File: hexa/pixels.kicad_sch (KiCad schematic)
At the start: 171 parts

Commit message: make the lipo_parallel pcb taller to fit everything better; lipo_parallel layout concept for battery terminals on the same side - change pin-matchups to work with that better; make motionhexa larger (more pixels) to accomodate that and bc more pixels = better; insert some capacitors with layout script
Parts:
- removed D76, D77, D78, D79: SK9822-EC20, motionhexa:LED-SK9822-EC20, symbol motionhexa:LED-SK9822-EC20
- added C10, C11, C12, C3, C4, C5, C6, C7, C8, C9: 1u, Capacitor_SMD:C_0402_1005Metric, symbol Device:C_Small
- added D166, D167, D168, D169, D170, D171, D172, D173, D174, D175, D176, D177, D178, D179, D180, D181, D182, D183, D184, D185, D186, D187, D188, D189, D190, D191, D192, D193, D194, D195, D196, D197, D198, D199, D200, D201, D202, D203, D204, D205, D206, D207, D208, D209, D210, D211, D212, D213, D214, D215, D216, D217, D218, D219, D220, D221, D222, D223, D224, D225, D226, D227, D228, D229, D230, D231, D232, D233, D234, D235, D236, D237, D238, D239, D240, D241, D242, D243, D244, D245, D246, D247, D248, D249, D250, D251, D252, D253, D254, D255, D256, D257, D258, D259, D260, D261, D262, D263, D264, D265, D266, D267, D268, D269, D270, D271: SK9822-EC20, motionhexa:LED-SK9822-EC20, symbol motionhexa:LED-SK9822-EC20
- C20, C21: value 10u -> 1u
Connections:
- net +5V: now also C10.1, C11.1, C12.1, C3.1, C4.1, C5.1, C6.1, C7.1, C8.1, C9.1, D166.5 (VDD), D167.5 (VDD), D168.5 (VDD), D169.5 (VDD), D170.5 (VDD), D171.5 (VDD), D172.5 (VDD), D173.5 (VDD), D174.5 (VDD), D175.5 (VDD), D176.5 (VDD), D177.5 (VDD), D178.5 (VDD), D179.5 (VDD), D180.5 (VDD), D181.5 (VDD), D182.5 (VDD), D183.5 (VDD), D184.5 (VDD), D185.5 (VDD), D186.5 (VDD), D187.5 (VDD), D188.5 (VDD), D189.5 (VDD), D190.5 (VDD), D191.5 (VDD), D192.5 (VDD), D193.5 (VDD), D194.5 (VDD), D195.5 (VDD)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
- net GND: now also C10.2, C11.2, C12.2, C3.2, C4.2, C5.2, C6.2, C7.2, C8.2, C9.2, D166.2 (GND), D167.2 (GND), D168.2 (GND), D169.2 (GND), D170.2 (GND), D171.2 (GND), D172.2 (GND), D173.2 (GND), D174.2 (GND), D175.2 (GND), D176.2 (GND), D177.2 (GND), D178.2 (GND), D179.2 (GND), D180.2 (GND), D181.2 (GND), D182.2 (GND), D183.2 (GND), D184.2 (GND), D185.2 (GND), D186.2 (GND), D187.2 (GND), D188.2 (GND), D189.2 (GND), D190.2 (GND), D191.2 (GND), D192.2 (GND), D193.2 (GND), D194.2 (GND), D195.2 (GND)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
- net at D75.1 (SDO): now also D166.3 (SDI)
- net at D75.6 (CKO): now also D166.4 (CKI)
- new net: D250.1 (SDO), D251.3 (SDI)
- new net: D249.1 (SDO), D250.3 (SDI)
- new net: D249.6 (CKO), D250.4 (CKI)
- new net: D250.6 (CKO), D251.4 (CKI)
- new net: D176.1 (SDO), D177.3 (SDI)
- new net: D175.1 (SDO), D176.3 (SDI)
- new net: D175.6 (CKO), D176.4 (CKI)
- new net: D176.6 (CKO), D177.4 (CKI)
- new net: D168.1 (SDO), D169.3 (SDI)
- new net: D167.1 (SDO), D168.3 (SDI)
- new net: D167.6 (CKO), D168.4 (CKI)
- new net: D168.6 (CKO), D169.4 (CKI)
- new net: D195.1 (SDO), D196.3 (SDI)
- new net: D194.1 (SDO), D195.3 (SDI)
- new net: D194.6 (CKO), D195.4 (CKI)
- new net: D195.6 (CKO), D196.4 (CKI)
- new net: D191.1 (SDO), D192.3 (SDI)
- new net: D190.1 (SDO), D191.3 (SDI)
- new net: D190.6 (CKO), D191.4 (CKI)
- new net: D191.6 (CKO), D192.4 (CKI)
- new net: D229.1 (SDO), D230.3 (SDI)
- new net: D228.1 (SDO), D229.3 (SDI)
- new net: D228.6 (CKO), D229.4 (CKI)
- new net: D229.6 (CKO), D230.4 (CKI)
- new net: D204.1 (SDO), D205.3 (SDI)
- new net: D203.1 (SDO), D204.3 (SDI)
- new net: D203.6 (CKO), D204.4 (CKI)
- new net: D204.6 (CKO), D205.4 (CKI)
- new net: D237.1 (SDO), D238.3 (SDI)
- new net: D236.1 (SDO), D237.3 (SDI)
- new net: D236.6 (CKO), D237.4 (CKI)
- new net: D237.6 (CKO), D238.4 (CKI)
- new net: D182.1 (SDO), D183.3 (SDI)
- new net: D181.1 (SDO), D182.3 (SDI)
- new net: D181.6 (CKO), D182.4 (CKI)
- new net: D182.6 (CKO), D183.4 (CKI)
- new net: D262.1 (SDO), D263.3 (SDI)
- new net: D261.1 (SDO), D262.3 (SDI)
- new net: D261.6 (CKO), D262.4 (CKI)
- new net: D262.6 (CKO), D263.4 (CKI)
- new net: D227.1 (SDO), D228.3 (SDI)
- new net: D227.6 (CKO), D228.4 (CKI)
- new net: D189.1 (SDO), D190.3 (SDI)
- new net: D189.6 (CKO), D190.4 (CKI)
- new net: D251.1 (SDO), D252.3 (SDI)
- new net: D251.6 (CKO), D252.4 (CKI)
- new net: D208.1 (SDO), D209.3 (SDI)
- new net: D207.1 (SDO), D208.3 (SDI)
- new net: D207.6 (CKO), D208.4 (CKI)
- new net: D208.6 (CKO), D209.4 (CKI)
- new net: D263.1 (SDO), D264.3 (SDI)
- new net: D263.6 (CKO), D264.4 (CKI)
- new net: D180.1 (SDO), D181.3 (SDI)
- new net: D179.1 (SDO), D180.3 (SDI)
- new net: D179.6 (CKO), D180.4 (CKI)
- new net: D180.6 (CKO), D181.4 (CKI)
- new net: D174.1 (SDO), D175.3 (SDI)
- new net: D173.1 (SDO), D174.3 (SDI)
- new net: D173.6 (CKO), D174.4 (CKI)
- new net: D174.6 (CKO), D175.4 (CKI)
- new net: D226.1 (SDO), D227.3 (SDI)
- new net: D225.1 (SDO), D226.3 (SDI)
- new net: D225.6 (CKO), D226.4 (CKI)
- new net: D226.6 (CKO), D227.4 (CKI)
- new net: D212.1 (SDO), D213.3 (SDI)
- new net: D211.1 (SDO), D212.3 (SDI)
- new net: D211.6 (CKO), D212.4 (CKI)
- new net: D212.6 (CKO), D213.4 (CKI)
- new net: D252.1 (SDO), D253.3 (SDI)
- new net: D252.6 (CKO), D253.4 (CKI)
- new net: D184.1 (SDO), D185.3 (SDI)
- new net: D183.1 (SDO), D184.3 (SDI)
- new net: D183.6 (CKO), D184.4 (CKI)
- new net: D184.6 (CKO), D185.4 (CKI)
- new net: D206.1 (SDO), D207.3 (SDI)
- new net: D206.6 (CKO), D207.4 (CKI)
- new net: D177.1 (SDO), D178.3 (SDI)
- new net: D177.6 (CKO), D178.4 (CKI)
- new net: D199.1 (SDO), D200.3 (SDI)
- new net: D198.1 (SDO), D199.3 (SDI)
- new net: D198.6 (CKO), D199.4 (CKI)
- new net: D199.6 (CKO), D200.4 (CKI)
- new net: D178.1 (SDO), D179.3 (SDI)
- new net: D178.6 (CKO), D179.4 (CKI)
- new net: D270.1 (SDO), D271.3 (SDI)
- new net: D269.1 (SDO), D270.3 (SDI)
- new net: D269.6 (CKO), D270.4 (CKI)
- new net: D270.6 (CKO), D271.4 (CKI)
- new net: D217.1 (SDO), D218.3 (SDI)
- new net: D216.1 (SDO), D217.3 (SDI)
- new net: D216.6 (CKO), D217.4 (CKI)
- new net: D217.6 (CKO), D218.4 (CKI)
- new net: D210.1 (SDO), D211.3 (SDI)
- new net: D210.6 (CKO), D211.4 (CKI)
- new net: D224.1 (SDO), D225.3 (SDI)
- new net: D224.6 (CKO), D225.4 (CKI)
- new net: D240.1 (SDO), D241.3 (SDI)
- new net: D239.1 (SDO), D240.3 (SDI)
- new net: D239.6 (CKO), D240.4 (CKI)
- new net: D240.6 (CKO), D241.4 (CKI)
- new net: D197.1 (SDO), D198.3 (SDI)
- new net: D197.6 (CKO), D198.4 (CKI)
- new net: D253.1 (SDO), D254.3 (SDI)
- new net: D253.6 (CKO), D254.4 (CKI)
- new net: D213.1 (SDO), D214.3 (SDI)
- new net: D213.6 (CKO), D214.4 (CKI)
- new net: D266.1 (SDO), D267.3 (SDI)
- new net: D265.1 (SDO), D266.3 (SDI)
- new net: D265.6 (CKO), D266.4 (CKI)
- new net: D266.6 (CKO), D267.4 (CKI)
- new net: D268.1 (SDO), D269.3 (SDI)
- new net: D268.6 (CKO), D269.4 (CKI)
- new net: D231.1 (SDO), D232.3 (SDI)
- new net: D230.1 (SDO), D231.3 (SDI)
- new net: D230.6 (CKO), D231.4 (CKI)
- new net: D231.6 (CKO), D232.4 (CKI)
- new net: D166.1 (SDO), D167.3 (SDI)
- new net: D166.6 (CKO), D167.4 (CKI)
- new net: D259.1 (SDO), D260.3 (SDI)
- new net: D258.1 (SDO), D259.3 (SDI)
- new net: D258.6 (CKO), D259.4 (CKI)
- new net: D259.6 (CKO), D260.4 (CKI)
- new net: D202.1 (SDO), D203.3 (SDI)
- new net: D201.1 (SDO), D202.3 (SDI)
- new net: D201.6 (CKO), D202.4 (CKI)
- new net: D202.6 (CKO), D203.4 (CKI)
- new net: D187.1 (SDO), D188.3 (SDI)
- new net: D186.1 (SDO), D187.3 (SDI)
- new net: D186.6 (CKO), D187.4 (CKI)
- new net: D187.6 (CKO), D188.4 (CKI)
- new net: D260.1 (SDO), D261.3 (SDI)
- new net: D260.6 (CKO), D261.4 (CKI)
- new net: D255.1 (SDO), D256.3 (SDI)
- new net: D254.1 (SDO), D255.3 (SDI)
- new net: D254.6 (CKO), D255.4 (CKI)
- new net: D255.6 (CKO), D256.4 (CKI)
- new net: D243.1 (SDO), D244.3 (SDI)
- new net: D242.1 (SDO), D243.3 (SDI)
- new net: D242.6 (CKO), D243.4 (CKI)
- new net: D243.6 (CKO), D244.4 (CKI)
- new net: D209.1 (SDO), D210.3 (SDI)
- new net: D209.6 (CKO), D210.4 (CKI)
- new net: D223.1 (SDO), D224.3 (SDI)
- new net: D223.6 (CKO), D224.4 (CKI)
- new net: D235.1 (SDO), D236.3 (SDI)
- new net: D234.1 (SDO), D235.3 (SDI)
- new net: D234.6 (CKO), D235.4 (CKI)
- new net: D235.6 (CKO), D236.4 (CKI)
- new net: D220.1 (SDO), D221.3 (SDI)
- new net: D219.1 (SDO), D220.3 (SDI)
- new net: D219.6 (CKO), D220.4 (CKI)
- new net: D220.6 (CKO), D221.4 (CKI)
- new net: D215.1 (SDO), D216.3 (SDI)
- new net: D215.6 (CKO), D216.4 (CKI)
- new net: D188.1 (SDO), D189.3 (SDI)
- new net: D188.6 (CKO), D189.4 (CKI)
- new net: D192.1 (SDO), D193.3 (SDI)
- new net: D192.6 (CKO), D193.4 (CKI)
- new net: D248.1 (SDO), D249.3 (SDI)
- new net: D247.1 (SDO), D248.3 (SDI)
- new net: D247.6 (CKO), D248.4 (CKI)
- new net: D248.6 (CKO), D249.4 (CKI)
- new net: D241.1 (SDO), D242.3 (SDI)
- new net: D241.6 (CKO), D242.4 (CKI)
- new net: D264.1 (SDO), D265.3 (SDI)
- new net: D264.6 (CKO), D265.4 (CKI)
- new net: D245.1 (SDO), D246.3 (SDI)
- new net: D244.1 (SDO), D245.3 (SDI)
- new net: D244.6 (CKO), D245.4 (CKI)
- new net: D245.6 (CKO), D246.4 (CKI)
- new net: D238.1 (SDO), D239.3 (SDI)
- new net: D238.6 (CKO), D239.4 (CKI)
- new net: D196.1 (SDO), D197.3 (SDI)
- new net: D196.6 (CKO), D197.4 (CKI)
- new net: D171.1 (SDO), D172.3 (SDI)
- new net: D170.1 (SDO), D171.3 (SDI)
- new net: D170.6 (CKO), D171.4 (CKI)
- new net: D171.6 (CKO), D172.4 (CKI)
- new net: D205.1 (SDO), D206.3 (SDI)
- new net: D205.6 (CKO), D206.4 (CKI)
- new net: D257.1 (SDO), D258.3 (SDI)
- new net: D257.6 (CKO), D258.4 (CKI)
- new net: D185.1 (SDO), D186.3 (SDI)
- new net: D185.6 (CKO), D186.4 (CKI)
- new net: D233.1 (SDO), D234.3 (SDI)
- new net: D232.1 (SDO), D233.3 (SDI)
- new net: D232.6 (CKO), D233.4 (CKI)
- new net: D233.6 (CKO), D234.4 (CKI)
- new net: D200.1 (SDO), D201.3 (SDI)
- new net: D200.6 (CKO), D201.4 (CKI)
- new net: D222.1 (SDO), D223.3 (SDI)
- new net: D222.6 (CKO), D223.4 (CKI)
- new net: D218.1 (SDO), D219.3 (SDI)
- new net: D218.6 (CKO), D219.4 (CKI)
- new net: D193.1 (SDO), D194.3 (SDI)
- new net: D193.6 (CKO), D194.4 (CKI)
- new net: D221.1 (SDO), D222.3 (SDI)
- new net: D221.6 (CKO), D222.4 (CKI)
- new net: D256.1 (SDO), D257.3 (SDI)
- new net: D256.6 (CKO), D257.4 (CKI)
- new net: D214.1 (SDO), D215.3 (SDI)
- new net: D214.6 (CKO), D215.4 (CKI)
- new net: D172.1 (SDO), D173.3 (SDI)
- new net: D172.6 (CKO), D173.4 (CKI)
- new net: D246.1 (SDO), D247.3 (SDI)
- new net: D246.6 (CKO), D247.4 (CKI)
- new net: D169.1 (SDO), D170.3 (SDI)
- new net: D169.6 (CKO), D170.4 (CKI)
- new net: D267.1 (SDO), D268.3 (SDI)
- new net: D267.6 (CKO), D268.4 (CKI)
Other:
- moved on the sheet: C20, C21

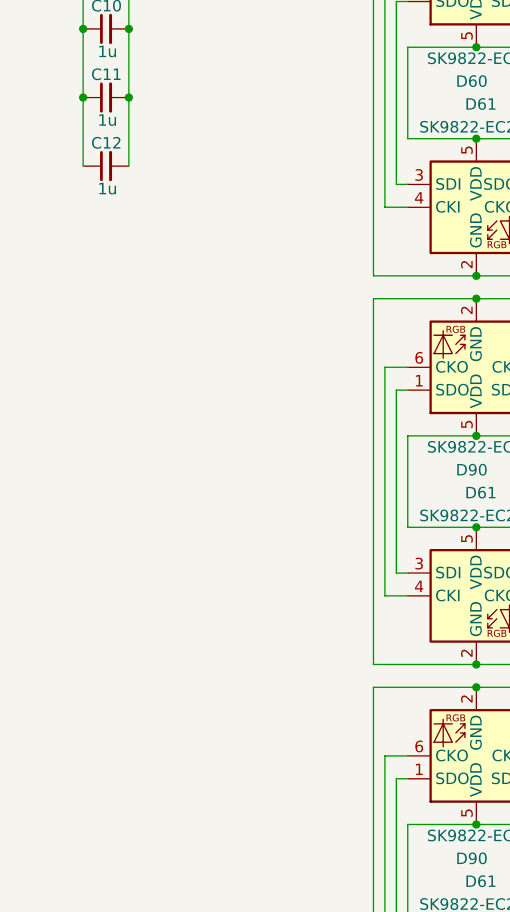
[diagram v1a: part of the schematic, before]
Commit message: add caps to schematic and script-wire up the power and gnd for each
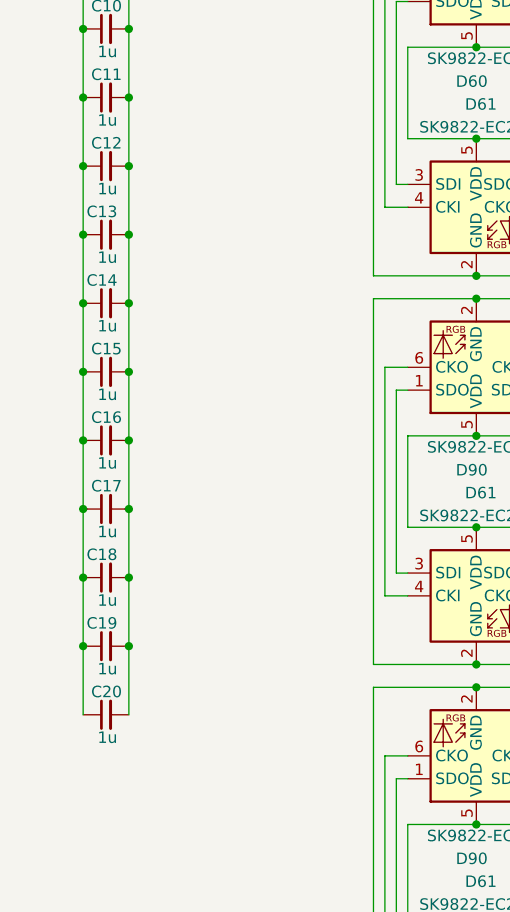
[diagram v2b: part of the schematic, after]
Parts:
- added C13, C14, C15, C16, C17, C18, C19, C20: 1u, Capacitor_SMD:C_0402_1005Metric, symbol Device:C_Small
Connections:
- net +5V: now also C13.1, C14.1, C15.1, C16.1, C17.1, C18.1, C19.1, C20.1
- net GND: now also C13.2, C14.2, C15.2, C16.2, C17.2, C18.2, C19.2, C20.2

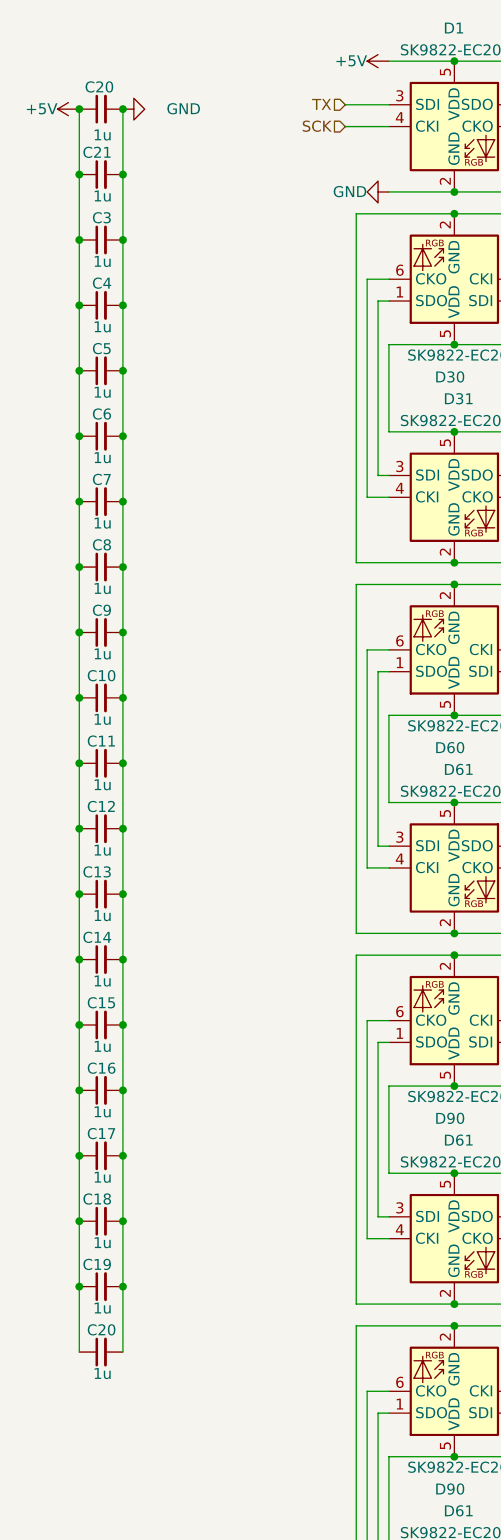
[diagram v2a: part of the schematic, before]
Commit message: ERC fixes
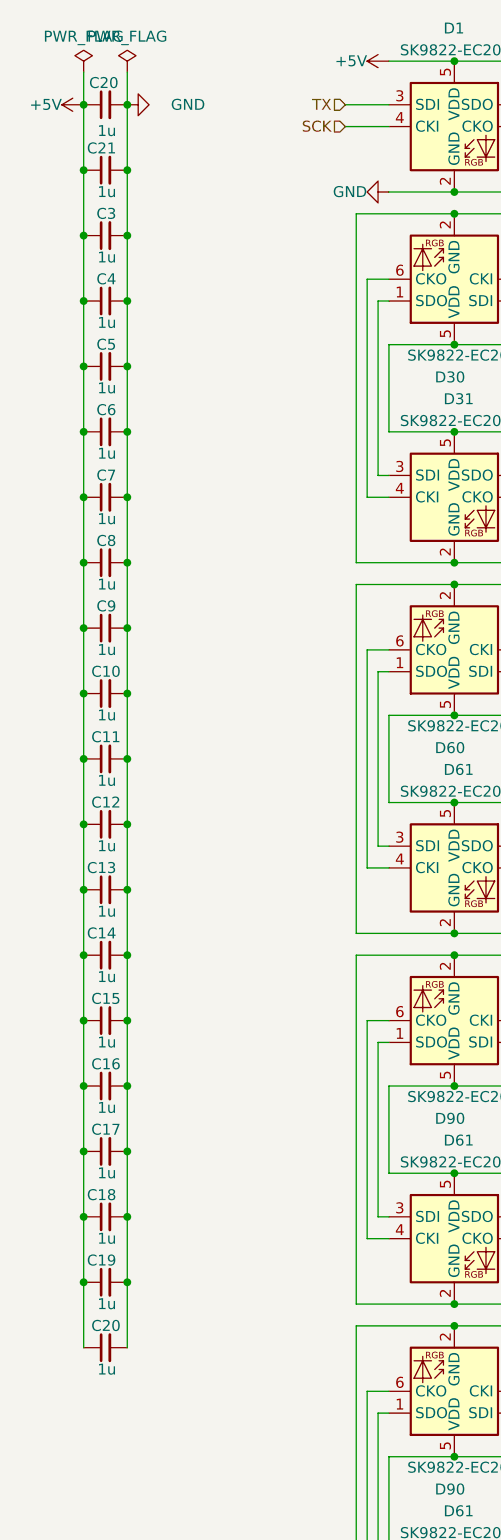
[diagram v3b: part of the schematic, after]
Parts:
- D1, D10, D11, D12, D13, D14, D15, D16, D166, D167, D168, D169, D17, D170, D171, D172, D173, D174, D175, D176, D177, D178, D179, D18, D180, D181, D182, D183, D184, D185, D186, D187, D188, D189, D19, D190, D191, D192, D193, D194, D195, D196, D197, D198, D199, D2, D20, D200, D201, D202, D203, D204, D205, D206, D207, D208, D209, D21, D210, D211, D212, D213, D214, D215, D216, D217, D218, D219, D22, D220, D221, D222, D223, D224, D225, D226, D227, D228, D229, D23, D230, D231, D232, D233, D234, D235, D236, D237, D238, D239, D24, D240, D241, D242, D243, D244, D245, D246, D247, D248, D249, D25, D250, D251, D252, D253, D254, D255, D256, D257, D258, D259, D26, D260, D261, D262, D263, D264, D265, D266, D267, D268, D269, D27, D270, D271, D28, D29, D3, D30, D31, D32, D33, D34, D35, D36, D37, D38, D39, D4, D40, D41, D42, D43, D44, D45, D46, D47, D48, D49, D5, D50, D51, D52, D53, D54, D55, D56, D57, D58, D59, D6, D60, D61, D62, D63, D64, D65, D66, D67, D68, D69, D7, D70, D71, D72, D73, D74, D75, D76, D77, D78, D79, D8, D80, D81, D82, D83, D84, D85, D86, D87, D88, D89, D9, D90: footprint motionhexa:LED-SK9822-EC20 -> LED_SMD:LED-APA102-2020
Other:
- moved on the sheet: C10, C11, C12, C13, C14, C15, C16, C17, C18, C19, C20, C21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

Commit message: fix most DRC issues
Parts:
- D1, D10, D11, D12, D13, D14, D15, D16, D166, D167, D168, D169, D17, D170, D171, D172, D173, D174, D175, D176, D177, D178, D179, D18, D180, D181, D182, D183, D184, D185, D186, D187, D188, D189, D19, D190, D191, D192, D193, D194, D195, D196, D197, D198, D199, D2, D20, D200, D201, D202, D203, D204, D205, D206, D207, D208, D209, D21, D210, D211, D212, D213, D214, D215, D216, D217, D218, D219, D22, D220, D221, D222, D223, D224, D225, D226, D227, D228, D229, D23, D230, D231, D232, D233, D234, D235, D236, D237, D238, D239, D24, D240, D241, D242, D243, D244, D245, D246, D247, D248, D249, D25, D250, D251, D252, D253, D254, D255, D256, D257, D258, D259, D26, D260, D261, D262, D263, D264, D265, D266, D267, D268, D269, D27, D270, D271, D28, D29, D3, D30, D31, D32, D33, D34, D35, D36, D37, D38, D39, D4, D40, D41, D42, D43, D44, D45, D46, D47, D48, D49, D5, D50, D51, D52, D53, D54, D55, D56, D57, D58, D59, D6, D60, D61, D62, D63, D64, D65, D66, D67, D68, D69, D7, D70, D71, D72, D73, D74, D75, D76, D77, D78, D79, D8, D80, D81, D82, D83, D84, D85, D86, D87, D88, D89, D9, D90: footprint LED_SMD:LED-APA102-2020 -> motionhexa:LED-SK9822-EC20

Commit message: add mount points to motionhexa; add some silkscreen; fix DRC errors
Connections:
- net +5V: now also D63.4 (CKI); no longer D166.5 (VDD), D167.5 (VDD), D168.5 (VDD), D169.5 (VDD), D170.5 (VDD), D171.5 (VDD), D172.5 (VDD), D173.5 (VDD), D174.5 (VDD), D175.5 (VDD), D176.5 (VDD), D177.5 (VDD), D178.5 (VDD), D179.5 (VDD), D180.5 (VDD), D181.5 (VDD), D182.5 (VDD), D183.5 (VDD), D184.5 (VDD), D185.5 (VDD), D186.5 (VDD), D187.5 (VDD), D188.5 (VDD), D189.5 (VDD), D190.5 (VDD), D191.5 (VDD), D192.5 (VDD), D193.5 (VDD), D194.5 (VDD), D195.5 (VDD), D196.5 (VDD), D197.5 (VDD), D198.5 (VDD), D199.5 (VDD), D200.5 (VDD), D201.5 (VDD), D202.5 (VDD), D203.5 (VDD), D204.5 (VDD), D205.5 (VDD)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
- net GND: now also D63.6 (CKO); no longer D166.2 (GND), D167.2 (GND), D168.2 (GND), D169.2 (GND), D170.2 (GND), D171.2 (GND), D172.2 (GND), D173.2 (GND), D174.2 (GND), D175.2 (GND), D176.2 (GND), D177.2 (GND), D178.2 (GND), D179.2 (GND), D180.2 (GND), D181.2 (GND), D182.2 (GND), D183.2 (GND), D184.2 (GND), D185.2 (GND), D186.2 (GND), D187.2 (GND), D188.2 (GND), D189.2 (GND), D190.2 (GND), D191.2 (GND), D192.2 (GND), D193.2 (GND), D194.2 (GND), D195.2 (GND), D196.2 (GND), D197.2 (GND), D198.2 (GND), D199.2 (GND), D200.2 (GND), D201.2 (GND), D202.2 (GND), D203.2 (GND), D204.2 (GND), D205.2 (GND)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
- net at D63.1 (SDO): now also D166.2 (GND), D167.2 (GND), D168.2 (GND), D169.2 (GND), D170.2 (GND), D171.2 (GND), D172.2 (GND), D173.2 (GND), D174.2 (GND), D175.2 (GND), D176.2 (GND), D177.2 (GND), D178.2 (GND), D179.2 (GND), D180.2 (GND), D181.2 (GND), D182.2 (GND), D183.2 (GND), D184.2 (GND), D185.2 (GND), D186.2 (GND), D187.2 (GND), D188.2 (GND), D189.2 (GND), D190.2 (GND), D191.2 (GND), D192.2 (GND), D193.2 (GND), D194.2 (GND), D195.2 (GND), D196.2 (GND), D197.2 (GND), D198.2 (GND), D199.2 (GND), D200.2 (GND), D201.2 (GND), D202.2 (GND), D203.2 (GND), D204.2 (GND), D205.2 (GND)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; no longer D64.3 (SDI)
- net at D64.4 (CKI): now also D63.5 (VDD); no longer D63.6 (CKO)
- net at D63.3 (SDI): now also D166.5 (VDD), D167.5 (VDD), D168.5 (VDD), D169.5 (VDD), D170.5 (VDD), D171.5 (VDD), D172.5 (VDD), D173.5 (VDD), D174.5 (VDD), D175.5 (VDD), D176.5 (VDD), D177.5 (VDD), D178.5 (VDD), D179.5 (VDD), D180.5 (VDD), D181.5 (VDD), D182.5 (VDD), D183.5 (VDD), D184.5 (VDD), D185.5 (VDD), D186.5 (VDD), D187.5 (VDD), D188.5 (VDD), D189.5 (VDD), D190.5 (VDD), D191.5 (VDD), D192.5 (VDD), D193.5 (VDD), D194.5 (VDD), D195.5 (VDD), D196.5 (VDD), D197.5 (VDD), D198.5 (VDD), D199.5 (VDD), D200.5 (VDD), D201.5 (VDD), D202.5 (VDD), D203.5 (VDD), D204.5 (VDD), D205.5 (VDD)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; no longer D62.1 (SDO)
- net at D62.6 (CKO): now also D63.2 (GND); no longer D63.4 (CKI)
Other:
- moved on the sheet: D63
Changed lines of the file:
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@@
   (junction (at -2.54 137.16) (diameter 0) (color 0 0 0 0)
   )
-  (junction (at 66.04 111.76) (diameter 0) (color 0 0 0 0)
-  )
   (junction (at 218.44 68.58) (diameter 0) (color 0 0 0 0)
   )
@@
   (junction (at 50.8 58.42) (diameter 0) (color 0 0 0 0)
   )
-  (junction (at 66.04 127) (diameter 0) (color 0 0 0 0)
-  )
   (junction (at 127 274.32) (diameter 0) (color 0 0 0 0)
   )
@@
     (stroke (width 0) (type default))
   )
+  (wire (pts (xy 68.58 111.76) (xy 81.28 111.76))
+    (stroke (width 0) (type default))
+  )
   (wire (pts (xy 142.24 187.96) (xy 157.48 187.96))
     (stroke (width 0) (type default))
@@
     (stroke (width 0) (type default))
   )
+  (wire (pts (xy 68.58 127) (xy 81.28 127))
+    (stroke (width 0) (type default))
+  )
   (wire (pts (xy 172.72 241.3) (xy 187.96 241.3))
     (stroke (width 0) (type default))
@@
     (stroke (width 0) (type default))
   )
-  (wire (pts (xy 66.04 127) (xy 81.28 127))
-    (stroke (width 0) (type default))
-  )
   (wire (pts (xy 111.76 345.44) (xy 127 345.44))
     (stroke (width 0) (type default))
@@
     (stroke (width 0) (type default))
   )
-  (wire (pts (xy 66.04 111.76) (xy 81.28 111.76))
-    (stroke (width 0) (type default))
-  )
   (wire (pts (xy 203.2 215.9) (xy 218.44 215.9))
     (stroke (width 0) (type default))
@@
     )
   )
-  (symbol (lib_id "motionhexa:LED-SK9822-EC20") (at 66.04 119.38 0) (unit 1)
+  (symbol (lib_id "motionhexa:LED-SK9822-EC20") (at 66.04 119.38 270) (unit 1)
     (in_bom yes) (on_board yes) (dnp no)
-    (property "Reference" "D63" (at 64.77 107.95 0)
+    (property "Reference" "D63" (at 77.47 118.11 0)
       (effects (font (size 1.27 1.27)) (justify left))
     )
-    (property "Value" "SK9822-EC20" (at 59.69 110.49 0)
+    (property "Value" "SK9822-EC20" (at 74.93 113.03 0)
       (effects (font (size 1.27 1.27)) (justify left))
     )
-    (property "Footprint" "motionhexa:LED-SK9822-EC20" (at 67.31 127 0)
+    (property "Footprint" "motionhexa:LED-SK9822-EC20" (at 58.42 120.65 0)
       (effects (font (size 1.27 1.27)) (justify left top) hide)
     )
-    (property "Datasheet" "http://www.normandled.com/upload/201906/EC20-9822(SK9822-2020)%20LED%20Datasheet.pdf" (at 68.58 128.905 0)
+    (property "Datasheet" "http://www.normandled.com/upload/201906/EC20-9822(SK9822-2020)%20LED%20Datasheet.pdf" (at 56.515 121.92 0)
       (effects (font (size 1.27 1.27)) (justify left top) hide)
     )

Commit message: power switch now controls OTG pin only, expectatio is that power consumption will be low enough with this PP; footprint for new power switch; updates to no longer export OTG pin; export SYS pin instead with no plan to use it
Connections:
- net +5V: now also D166.5 (VDD), D167.5 (VDD), D168.5 (VDD), D169.5 (VDD), D170.5 (VDD), D171.5 (VDD), D172.5 (VDD), D173.5 (VDD), D174.5 (VDD), D175.5 (VDD), D176.5 (VDD), D177.5 (VDD), D178.5 (VDD), D179.5 (VDD), D180.5 (VDD), D181.5 (VDD), D182.5 (VDD), D183.5 (VDD), D184.5 (VDD), D185.5 (VDD), D186.5 (VDD), D187.5 (VDD), D188.5 (VDD), D189.5 (VDD), D190.5 (VDD), D191.5 (VDD), D192.5 (VDD), D193.5 (VDD), D194.5 (VDD), D195.5 (VDD), D196.5 (VDD), D197.5 (VDD), D198.5 (VDD), D199.5 (VDD), D200.5 (VDD), D201.5 (VDD), D202.5 (VDD), D203.5 (VDD), D204.5 (VDD), D205.5 (VDD), D206.5 (VDD), D207.5 (VDD), D208.5 (VDD), D209.5 (VDD), D210.5 (VDD), D211.5 (VDD), D212.5 (VDD), D213.5 (VDD), D214.5 (VDD), D215.5 (VDD), D216.5 (VDD), D217.5 (VDD), D218.5 (VDD), D219.5 (VDD), D220.5 (VDD), D221.5 (VDD), D222.5 (VDD), D223.5 (VDD), D224.5 (VDD), D225.5 (VDD), D226.5 (VDD), D227.5 (VDD), D228.5 (VDD), D229.5 (VDD), D230.5 (VDD), D231.5 (VDD), D232.5 (VDD), D233.5 (VDD), D234.5 (VDD), D235.5 (VDD), D236.5 (VDD), D237.5 (VDD), D238.5 (VDD), D239.5 (VDD), D240.5 (VDD), D241.5 (VDD), D242.5 (VDD), D243.5 (VDD), D244.5 (VDD), D245.5 (VDD), D246.5 (VDD), D247.5 (VDD), D248.5 (VDD), D249.5 (VDD), D250.5 (VDD), D251.5 (VDD), D252.5 (VDD), D253.5 (VDD), D254.5 (VDD), D255.5 (VDD), D256.5 (VDD), D257.5 (VDD), D258.5 (VDD), D259.5 (VDD), D260.5 (VDD), D261.5 (VDD), D262.5 (VDD), D263.5 (VDD), D264.5 (VDD), D265.5 (VDD), D266.5 (VDD), D267.5 (VDD), D268.5 (VDD), D269.5 (VDD), D270.5 (VDD), D271.5 (VDD), D61.5 (VDD), D61.5 (VDD), D61.5 (VDD), D62.5 (VDD), D62.5 (VDD), D62.5 (VDD), D63.5 (VDD), D63.5 (VDD), D63.5 (VDD), D63.5 (VDD), D64.5 (VDD), D64.5 (VDD), D64.5 (VDD), D64.5 (VDD), D65.5 (VDD), D65.5 (VDD), D65.5 (VDD), D65.5 (VDD), D66.5 (VDD), D66.5 (VDD), D66.5 (VDD), D66.5 (VDD), D67.5 (VDD), D67.5 (VDD), D67.5 (VDD), D67.5 (VDD), D68.5 (VDD), D68.5 (VDD), D68.5 (VDD), D68.5 (VDD), D69.5 (VDD), D69.5 (VDD), D69.5 (VDD), D69.5 (VDD), D70.5 (VDD), D70.5 (VDD), D70.5 (VDD), D70.5 (VDD), D71.5 (VDD), D71.5 (VDD), D71.5 (VDD), D71.5 (VDD), D72.5 (VDD), D72.5 (VDD), D72.5 (VDD), D72.5 (VDD), D73.5 (VDD), D73.5 (VDD), D73.5 (VDD), D73.5 (VDD), D74.5 (VDD), D74.5 (VDD), D74.5 (VDD), D74.5 (VDD), D75.5 (VDD), D75.5 (VDD), D75.5 (VDD), D75.5 (VDD), D76.5 (VDD), D76.5 (VDD), D76.5 (VDD), D77.5 (VDD), D77.5 (VDD), D77.5 (VDD), D78.5 (VDD), D78.5 (VDD), D78.5 (VDD), D79.5 (VDD), D79.5 (VDD), D79.5 (VDD), D80.5 (VDD), D80.5 (VDD), D80.5 (VDD), D81.5 (VDD), D81.5 (VDD), D81.5 (VDD), D82.5 (VDD), D82.5 (VDD), D82.5 (VDD), D83.5 (VDD), D83.5 (VDD), D83.5 (VDD), D84.5 (VDD), D84.5 (VDD), D84.5 (VDD), D85.5 (VDD), D85.5 (VDD), D85.5 (VDD), D86.5 (VDD), D86.5 (VDD), D86.5 (VDD), D87.5 (VDD), D87.5 (VDD), D87.5 (VDD), D88.5 (VDD), D88.5 (VDD), D88.5 (VDD), D89.5 (VDD), D89.5 (VDD), D89.5 (VDD), D90.5 (VDD), D90.5 (VDD), D90.5 (VDD); no longer D63.4 (CKI)
- net GND: now also D166.2 (GND), D167.2 (GND), D168.2 (GND), D169.2 (GND), D170.2 (GND), D171.2 (GND), D172.2 (GND), D173.2 (GND), D174.2 (GND), D175.2 (GND), D176.2 (GND), D177.2 (GND), D178.2 (GND), D179.2 (GND), D180.2 (GND), D181.2 (GND), D182.2 (GND), D183.2 (GND), D184.2 (GND), D185.2 (GND), D186.2 (GND), D187.2 (GND), D188.2 (GND), D189.2 (GND), D190.2 (GND), D191.2 (GND), D192.2 (GND), D193.2 (GND), D194.2 (GND), D195.2 (GND), D196.2 (GND), D197.2 (GND), D198.2 (GND), D199.2 (GND), D200.2 (GND), D201.2 (GND), D202.2 (GND), D203.2 (GND), D204.2 (GND), D205.2 (GND), D206.2 (GND), D207.2 (GND), D208.2 (GND), D209.2 (GND), D210.2 (GND), D211.2 (GND), D212.2 (GND), D213.2 (GND), D214.2 (GND), D215.2 (GND), D216.2 (GND), D217.2 (GND), D218.2 (GND), D219.2 (GND), D220.2 (GND), D221.2 (GND), D222.2 (GND), D223.2 (GND), D224.2 (GND), D225.2 (GND), D226.2 (GND), D227.2 (GND), D228.2 (GND), D229.2 (GND), D230.2 (GND), D231.2 (GND), D232.2 (GND), D233.2 (GND), D234.2 (GND), D235.2 (GND), D236.2 (GND), D237.2 (GND), D238.2 (GND), D239.2 (GND), D240.2 (GND), D241.2 (GND), D242.2 (GND), D243.2 (GND), D244.2 (GND), D245.2 (GND), D246.2 (GND), D247.2 (GND), D248.2 (GND), D249.2 (GND), D250.2 (GND), D251.2 (GND), D252.2 (GND), D253.2 (GND), D254.2 (GND), D255.2 (GND), D256.2 (GND), D257.2 (GND), D258.2 (GND), D259.2 (GND), D260.2 (GND), D261.2 (GND), D262.2 (GND), D263.2 (GND), D264.2 (GND), D265.2 (GND), D266.2 (GND), D267.2 (GND), D268.2 (GND), D269.2 (GND), D270.2 (GND), D271.2 (GND), D61.2 (GND), D61.2 (GND), D61.2 (GND), D62.2 (GND), D62.2 (GND), D62.2 (GND), D63.2 (GND), D63.2 (GND), D63.2 (GND), D63.2 (GND), D64.2 (GND), D64.2 (GND), D64.2 (GND), D64.2 (GND), D65.2 (GND), D65.2 (GND), D65.2 (GND), D65.2 (GND), D66.2 (GND), D66.2 (GND), D66.2 (GND), D66.2 (GND), D67.2 (GND), D67.2 (GND), D67.2 (GND), D67.2 (GND), D68.2 (GND), D68.2 (GND), D68.2 (GND), D68.2 (GND), D69.2 (GND), D69.2 (GND), D69.2 (GND), D69.2 (GND), D70.2 (GND), D70.2 (GND), D70.2 (GND), D70.2 (GND), D71.2 (GND), D71.2 (GND), D71.2 (GND), D71.2 (GND), D72.2 (GND), D72.2 (GND), D72.2 (GND), D72.2 (GND), D73.2 (GND), D73.2 (GND), D73.2 (GND), D73.2 (GND), D74.2 (GND), D74.2 (GND), D74.2 (GND), D74.2 (GND), D75.2 (GND), D75.2 (GND), D75.2 (GND), D75.2 (GND), D76.2 (GND), D76.2 (GND), D76.2 (GND), D77.2 (GND), D77.2 (GND), D77.2 (GND), D78.2 (GND), D78.2 (GND), D78.2 (GND), D79.2 (GND), D79.2 (GND), D79.2 (GND), D80.2 (GND), D80.2 (GND), D80.2 (GND), D81.2 (GND), D81.2 (GND), D81.2 (GND), D82.2 (GND), D82.2 (GND), D82.2 (GND), D83.2 (GND), D83.2 (GND), D83.2 (GND), D84.2 (GND), D84.2 (GND), D84.2 (GND), D85.2 (GND), D85.2 (GND), D85.2 (GND), D86.2 (GND), D86.2 (GND), D86.2 (GND), D87.2 (GND), D87.2 (GND), D87.2 (GND), D88.2 (GND), D88.2 (GND), D88.2 (GND), D89.2 (GND), D89.2 (GND), D89.2 (GND), D90.2 (GND), D90.2 (GND), D90.2 (GND); no longer D63.6 (CKO)
- net at D64.3 (SDI): now also D63.1 (SDO)
- net at D64.4 (CKI): now also D63.6 (CKO); no longer D63.5 (VDD)
- net at D62.6 (CKO): now also D63.4 (CKI); no longer D63.2 (GND)
- net at D62.1 (SDO): now also D63.3 (SDI)
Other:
- moved on the sheet: D63
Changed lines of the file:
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@@
   (junction (at 35.56 187.96) (diameter 0) (color 0 0 0 0)
   )
+  (junction (at 66.04 127) (diameter 0) (color 0 0 0 0)
+  )
   (junction (at 81.28 187.96) (diameter 0) (color 0 0 0 0)
   )
@@
   (junction (at 157.48 198.12) (diameter 0) (color 0 0 0 0)
   )
+  (junction (at 66.04 111.76) (diameter 0) (color 0 0 0 0)
+  )
   (junction (at 172.72 256.54) (diameter 0) (color 0 0 0 0)
   )
@@
     (stroke (width 0) (type default))
   )
-  (wire (pts (xy 68.58 111.76) (xy 81.28 111.76))
+  (wire (pts (xy 66.04 111.76) (xy 81.28 111.76))
     (stroke (width 0) (type default))
   )
@@
     (stroke (width 0) (type default))
   )
-  (wire (pts (xy 68.58 127) (xy 81.28 127))
+  (wire (pts (xy 66.04 127) (xy 81.28 127))
     (stroke (width 0) (type default))
   )
@@
     )
   )
-  (symbol (lib_id "motionhexa:LED-SK9822-EC20") (at 66.04 119.38 270) (unit 1)
+  (symbol (lib_id "motionhexa:LED-SK9822-EC20") (at 66.04 119.38 0) (unit 1)
     (in_bom yes) (on_board yes) (dnp no)
-    (property "Reference" "D63" (at 77.47 118.11 0)
+    (property "Reference" "D63" (at 64.77 107.95 0)
       (effects (font (size 1.27 1.27)) (justify left))
     )
-    (property "Value" "SK9822-EC20" (at 74.93 113.03 0)
+    (property "Value" "SK9822-EC20" (at 59.69 110.49 0)
       (effects (font (size 1.27 1.27)) (justify left))
     )
-    (property "Footprint" "motionhexa:LED-SK9822-EC20" (at 58.42 120.65 0)
+    (property "Footprint" "motionhexa:LED-SK9822-EC20" (at 67.31 127 0)
       (effects (font (size 1.27 1.27)) (justify left top) hide)
     )
-    (property "Datasheet" "http://www.normandled.com/upload/201906/EC20-9822(SK9822-2020)%20LED%20Datasheet.pdf" (at 56.515 121.92 0)
+    (property "Datasheet" "http://www.normandled.com/upload/201906/EC20-9822(SK9822-2020)%20LED%20Datasheet.pdf" (at 68.58 128.905 0)
       (effects (font (size 1.27 1.27)) (justify left top) hide)
     )
